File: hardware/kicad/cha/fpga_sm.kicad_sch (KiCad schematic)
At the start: 26 parts, among them J3 CONF SM, U14 iCE40HX4K-TQ144, X2 25 MHz 3,3 V

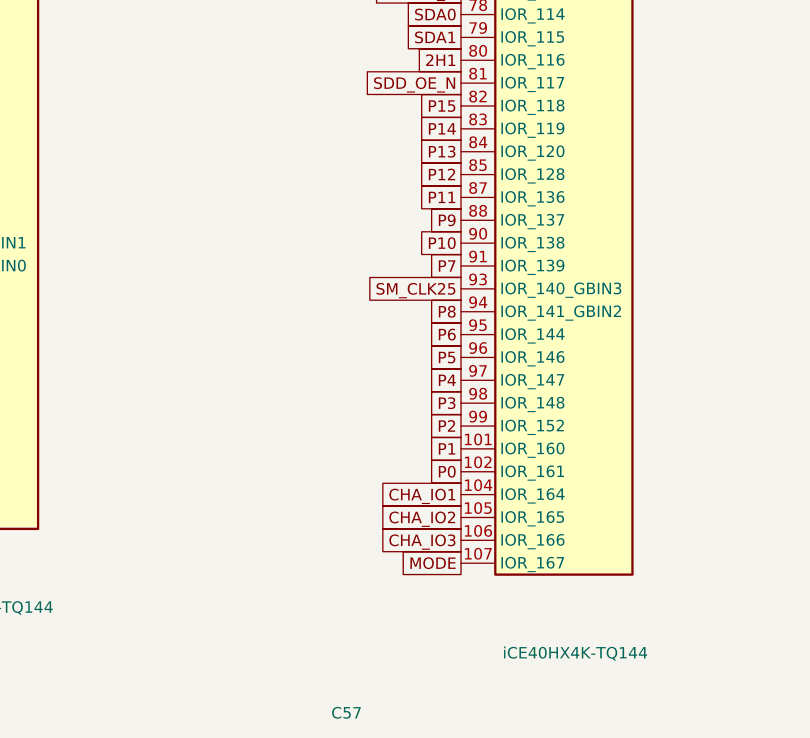
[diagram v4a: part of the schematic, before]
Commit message: Pico 2, microSD et bouton sur la carte PROG ; pistes d'alimentation larges
- La carte PROG est côté avant de la cartouche, composants vers l'avant :
  lecteur microSD et bouton accessibles. Le câble PROG-CHA porte
  désormais le bus de liaison C/SM ; connecteur au même endroit sur les
  deux cartes (x = 172 mm), prêt pour un connecteur carte à carte.
- Sous le Pico : ni piste ni via sur la face composants (pastilles de
  test nues sous le module).
- Classes de réseaux écrites dans le .kicad_pro : +5V et VSYS en 0,5 mm,
  +1V2 en 0,3 mm.
- Broches des FPGA réoptimisées ; contrôle Freerouting sans violation ;
  routage des deux cartes et vérification de timing en cours.

Co-Authored-By: Claude Opus 5.5 <noreply@anthropic.com>
Claude-Session: https://claude.ai/code/session_01WKfXP1YJ8otGxZ5dsY6Agh
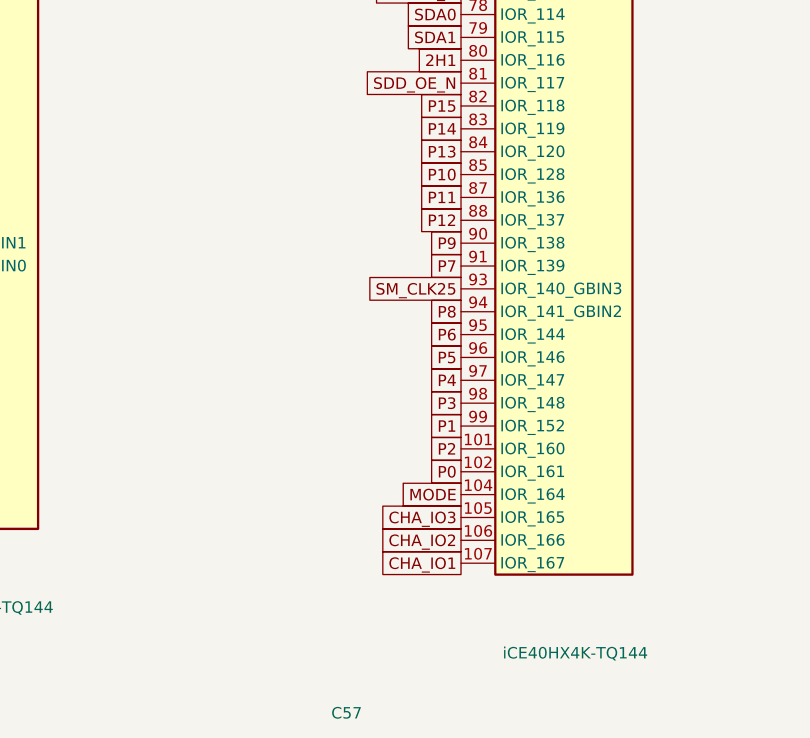
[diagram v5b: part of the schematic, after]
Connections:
- net CHA_IO1: now also U14.107 (IOR_167); no longer U14.104 (IOR_164)
- net CHA_IO2: now also U14.106 (IOR_166); no longer U14.105 (IOR_165)
- net CHA_IO3: now also U14.105 (IOR_165); no longer U14.106 (IOR_166)
- net MODE: now also U14.104 (IOR_164); no longer U14.107 (IOR_167)
- net P1: now also U14.99 (IOR_152); no longer U14.101 (IOR_160)
- net P10: now also U14.85 (IOR_128); no longer U14.90 (IOR_138)
- net P12: now also U14.88 (IOR_137); no longer U14.85 (IOR_128)
- net P2: now also U14.101 (IOR_160); no longer U14.99 (IOR_152)
- net P9: now also U14.90 (IOR_138); no longer U14.88 (IOR_137)
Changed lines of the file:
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@@
     (instances
       (project "cha"
-        (path "/c2acc1ad-3350-4022-8990-314ed37b470d/7c17e6ce-3dc1-4363-ae9a-1efd42617669"
+        (path "/e0c94673-4de7-4c3d-ae38-3ad172bd9211/19c2e398-814e-49a6-a22b-587549b2e82f"
           (reference "U14")
           (unit 1)))))
@@
     (instances
       (project "cha"
-        (path "/c2acc1ad-3350-4022-8990-314ed37b470d/7c17e6ce-3dc1-4363-ae9a-1efd42617669"
+        (path "/e0c94673-4de7-4c3d-ae38-3ad172bd9211/19c2e398-814e-49a6-a22b-587549b2e82f"
           (reference "U14")
           (unit 2)))))
@@
         (font
           (size 1.27 1.27)) hide)))
-  (global_label "P1"
+  (global_label "P2"
     (shape passive)
     (at 121.92 111.76 180)
@@
         (font
           (size 1.27 1.27)) hide)))
-  (global_label "CHA_IO1"
+  (global_label "MODE"
     (shape passive)
     (at 121.92 116.84 180)
@@
         (font
           (size 1.27 1.27)) hide)))
-  (global_label "CHA_IO2"
+  (global_label "CHA_IO3"
     (shape passive)
     (at 121.92 119.38 180)
@@
         (font
           (size 1.27 1.27)) hide)))
-  (global_label "CHA_IO3"
+  (global_label "CHA_IO2"
     (shape passive)
     (at 121.92 121.92 180)
@@
         (font
           (size 1.27 1.27)) hide)))
-  (global_label "MODE"
+  (global_label "CHA_IO1"
     (shape passive)
     (at 121.92 124.46 180)
@@
         (font
           (size 1.27 1.27)) hide)))
-  (global_label "P12"
+  (global_label "P10"
     (shape passive)
     (at 121.92 81.28 180)
@@
         (font
           (size 1.27 1.27)) hide)))
-  (global_label "P9"
+  (global_label "P12"
     (shape passive)
     (at 121.92 86.36 180)
@@
         (font
           (size 1.27 1.27)) hide)))
-  (global_label "P10"
+  (global_label "P9"
     (shape passive)
     (at 121.92 88.9 180)
@@
         (font
           (size 1.27 1.27)) hide)))
-  (global_label "P2"
+  (global_label "P1"
     (shape passive)
     (at 121.92 109.22 180)
@@
     (instances
       (project "cha"
-        (path "/c2acc1ad-3350-4022-8990-314ed37b470d/7c17e6ce-3dc1-4363-ae9a-1efd42617669"
+        (path "/e0c94673-4de7-4c3d-ae38-3ad172bd9211/19c2e398-814e-49a6-a22b-587549b2e82f"
           (reference "U14")
           (unit 3)))))
@@
     (instances
       (project "cha"
-        (path "/c2acc1ad-3350-4022-8990-314ed37b470d/7c17e6ce-3dc1-4363-ae9a-1efd42617669"
+        (path "/e0c94673-4de7-4c3d-ae38-3ad172bd9211/19c2e398-814e-49a6-a22b-587549b2e82f"
           (reference "U14")
           (unit 4)))))
@@
     (instances
       (project "cha"
-        (path "/c2acc1ad-3350-4022-8990-314ed37b470d/7c17e6ce-3dc1-4363-ae9a-1efd42617669"
+        (path "/e0c94673-4de7-4c3d-ae38-3ad172bd9211/19c2e398-814e-49a6-a22b-587549b2e82f"
           (reference "U14")
           (unit 5)))))
@@
     (instances
       (project "cha"
-        (path "/c2acc1ad-3350-4022-8990-314ed37b470d/7c17e6ce-3dc1-4363-ae9a-1efd42617669"
+        (path "/e0c94673-4de7-4c3d-ae38-3ad172bd9211/19c2e398-814e-49a6-a22b-587549b2e82f"
           (reference "C50")
           (unit 1)))))
@@
     (instances
       (project "cha"
-        (path "/c2acc1ad-3350-4022-8990-314ed37b470d/7c17e6ce-3dc1-4363-ae9a-1efd42617669"
+        (path "/e0c94673-4de7-4c3d-ae38-3ad172bd9211/19c2e398-814e-49a6-a22b-587549b2e82f"
           (reference "C51")
           (unit 1)))))
@@
     (instances
       (project "cha"
-        (path "/c2acc1ad-3350-4022-8990-314ed37b470d/7c17e6ce-3dc1-4363-ae9a-1efd42617669"
+        (path "/e0c94673-4de7-4c3d-ae38-3ad172bd9211/19c2e398-814e-49a6-a22b-587549b2e82f"
           (reference "C52")
           (unit 1)))))
@@
     (instances
       (project "cha"
-        (path "/c2acc1ad-3350-4022-8990-314ed37b470d/7c17e6ce-3dc1-4363-ae9a-1efd42617669"
+        (path "/e0c94673-4de7-4c3d-ae38-3ad172bd9211/19c2e398-814e-49a6-a22b-587549b2e82f"
           (reference "C53")
           (unit 1)))))
@@
     (instances
       (project "cha"
-        (path "/c2acc1ad-3350-4022-8990-314ed37b470d/7c17e6ce-3dc1-4363-ae9a-1efd42617669"
+        (path "/e0c94673-4de7-4c3d-ae38-3ad172bd9211/19c2e398-814e-49a6-a22b-587549b2e82f"
           (reference "C54")
           (unit 1)))))
@@
     (instances
       (project "cha"
-        (path "/c2acc1ad-3350-4022-8990-314ed37b470d/7c17e6ce-3dc1-4363-ae9a-1efd42617669"
+        (path "/e0c94673-4de7-4c3d-ae38-3ad172bd9211/19c2e398-814e-49a6-a22b-587549b2e82f"
           (reference "C55")
           (unit 1)))))
@@
     (instances
       (project "cha"
-        (path "/c2acc1ad-3350-4022-8990-314ed37b470d/7c17e6ce-3dc1-4363-ae9a-1efd42617669"
+        (path "/e0c94673-4de7-4c3d-ae38-3ad172bd9211/19c2e398-814e-49a6-a22b-587549b2e82f"
           (reference "C56")
           (unit 1)))))
@@
     (instances
       (project "cha"
-        (path "/c2acc1ad-3350-4022-8990-314ed37b470d/7c17e6ce-3dc1-4363-ae9a-1efd42617669"
+        (path "/e0c94673-4de7-4c3d-ae38-3ad172bd9211/19c2e398-814e-49a6-a22b-587549b2e82f"
           (reference "C57")
           (unit 1)))))
@@
     (instances
       (project "cha"
-        (path "/c2acc1ad-3350-4022-8990-314ed37b470d/7c17e6ce-3dc1-4363-ae9a-1efd42617669"
+        (path "/e0c94673-4de7-4c3d-ae38-3ad172bd9211/19c2e398-814e-49a6-a22b-587549b2e82f"
           (reference "C58")
           (unit 1)))))
@@
     (instances
       (project "cha"
-        (path "/c2acc1ad-3350-4022-8990-314ed37b470d/7c17e6ce-3dc1-4363-ae9a-1efd42617669"
+        (path "/e0c94673-4de7-4c3d-ae38-3ad172bd9211/19c2e398-814e-49a6-a22b-587549b2e82f"
           (reference "C59")
           (unit 1)))))
@@
     (instances
       (project "cha"
-        (path "/c2acc1ad-3350-4022-8990-314ed37b470d/7c17e6ce-3dc1-4363-ae9a-1efd42617669"
+        (path "/e0c94673-4de7-4c3d-ae38-3ad172bd9211/19c2e398-814e-49a6-a22b-587549b2e82f"
           (reference "C60")
           (unit 1)))))
@@
     (instances
       (project "cha"
-        (path "/c2acc1ad-3350-4022-8990-314ed37b470d/7c17e6ce-3dc1-4363-ae9a-1efd42617669"
+        (path "/e0c94673-4de7-4c3d-ae38-3ad172bd9211/19c2e398-814e-49a6-a22b-587549b2e82f"
           (reference "C61")
           (unit 1)))))
@@
     (instances
       (project "cha"
-        (path "/c2acc1ad-3350-4022-8990-314ed37b470d/7c17e6ce-3dc1-4363-ae9a-1efd42617669"
+        (path "/e0c94673-4de7-4c3d-ae38-3ad172bd9211/19c2e398-814e-49a6-a22b-587549b2e82f"
           (reference "C62")
           (unit 1)))))
@@
     (instances
       (project "cha"
-        (path "/c2acc1ad-3350-4022-8990-314ed37b470d/7c17e6ce-3dc1-4363-ae9a-1efd42617669"
+        (path "/e0c94673-4de7-4c3d-ae38-3ad172bd9211/19c2e398-814e-49a6-a22b-587549b2e82f"
           (reference "C63")
           (unit 1)))))
@@
     (instances
       (project "cha"
-        (path "/c2acc1ad-3350-4022-8990-314ed37b470d/7c17e6ce-3dc1-4363-ae9a-1efd42617669"
+        (path "/e0c94673-4de7-4c3d-ae38-3ad172bd9211/19c2e398-814e-49a6-a22b-587549b2e82f"
           (reference "C64")
           (unit 1)))))
@@
     (instances
       (project "cha"
-        (path "/c2acc1ad-3350-4022-8990-314ed37b470d/7c17e6ce-3dc1-4363-ae9a-1efd42617669"
+        (path "/e0c94673-4de7-4c3d-ae38-3ad172bd9211/19c2e398-814e-49a6-a22b-587549b2e82f"
           (reference "R10")
           (unit 1)))))
@@
     (instances
       (project "cha"
-        (path "/c2acc1ad-3350-4022-8990-314ed37b470d/7c17e6ce-3dc1-4363-ae9a-1efd42617669"
+        (path "/e0c94673-4de7-4c3d-ae38-3ad172bd9211/19c2e398-814e-49a6-a22b-587549b2e82f"
           (reference "C65")
           (unit 1)))))
@@
     (instances
       (project "cha"
-        (path "/c2acc1ad-3350-4022-8990-314ed37b470d/7c17e6ce-3dc1-4363-ae9a-1efd42617669"
+        (path "/e0c94673-4de7-4c3d-ae38-3ad172bd9211/19c2e398-814e-49a6-a22b-587549b2e82f"
           (reference "C66")
           (unit 1)))))
@@
     (instances
       (project "cha"
-        (path "/c2acc1ad-3350-4022-8990-314ed37b470d/7c17e6ce-3dc1-4363-ae9a-1efd42617669"
+        (path "/e0c94673-4de7-4c3d-ae38-3ad172bd9211/19c2e398-814e-49a6-a22b-587549b2e82f"
           (reference "R11")
           (unit 1)))))
@@
     (instances
       (project "cha"
-        (path "/c2acc1ad-3350-4022-8990-314ed37b470d/7c17e6ce-3dc1-4363-ae9a-1efd42617669"
+        (path "/e0c94673-4de7-4c3d-ae38-3ad172bd9211/19c2e398-814e-49a6-a22b-587549b2e82f"
           (reference "C67")
           (unit 1)))))
@@
     (instances
       (project "cha"
-        (path "/c2acc1ad-3350-4022-8990-314ed37b470d/7c17e6ce-3dc1-4363-ae9a-1efd42617669"
+        (path "/e0c94673-4de7-4c3d-ae38-3ad172bd9211/19c2e398-814e-49a6-a22b-587549b2e82f"
           (reference "C68")
           (unit 1)))))
@@
     (instances
       (project "cha"
-        (path "/c2acc1ad-3350-4022-8990-314ed37b470d/7c17e6ce-3dc1-4363-ae9a-1efd42617669"
+        (path "/e0c94673-4de7-4c3d-ae38-3ad172bd9211/19c2e398-814e-49a6-a22b-587549b2e82f"
           (reference "R12")
           (unit 1)))))
@@
     (instances
       (project "cha"
-        (path "/c2acc1ad-3350-4022-8990-314ed37b470d/7c17e6ce-3dc1-4363-ae9a-1efd42617669"
+        (path "/e0c94673-4de7-4c3d-ae38-3ad172bd9211/19c2e398-814e-49a6-a22b-587549b2e82f"
           (reference "J3")
           (unit 1)))))
@@
     (instances
       (project "cha"
-        (path "/c2acc1ad-3350-4022-8990-314ed37b470d/7c17e6ce-3dc1-4363-ae9a-1efd42617669"
+        (path "/e0c94673-4de7-4c3d-ae38-3ad172bd9211/19c2e398-814e-49a6-a22b-587549b2e82f"
           (reference "X2")
           (unit 1)))))
@@
     (instances
       (project "cha"
-        (path "/c2acc1ad-3350-4022-8990-314ed37b470d/7c17e6ce-3dc1-4363-ae9a-1efd42617669"
+        (path "/e0c94673-4de7-4c3d-ae38-3ad172bd9211/19c2e398-814e-49a6-a22b-587549b2e82f"
           (reference "C69")
           (unit 1)))))

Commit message: Régulateur 3,3 V à découpage, horloge SDRAM adaptée côté FPGA, U8 en 74AHCT125
- AP63203 (TSOT-23-6, sortie fixe 3,3 V, ~90 %) à la place de
  l'AMS1117 : ~0,15 W de pertes au lieu de ~0,75 W et moins de courant
  tiré sur le 5 V de la console ; L 4,7 µH, Cin 10 µF, Cout 2 x 22 µF.
- Résistance série de 33 ohms de l'horloge SDRAM déclarée avec le FPGA :
  placée à 2,7 mm de sa broche (au lieu de ~30 mm, côté SDRAM).
- CHA : U8 (16244 pour 2 canaux) remplacé par un 74AHCT125.
Cartes replacées, contrôle Freerouting sans violation ; routage des
deux cartes et vérification de timing en cours.

Co-Authored-By: Claude Opus 5.5 <noreply@anthropic.com>
Claude-Session: https://claude.ai/code/session_01WKfXP1YJ8otGxZ5dsY6Agh
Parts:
- removed C50: 100n, Capacitor_SMD:C_0603_1608Metric, symbol Device:C
- added C70: 100n, Capacitor_SMD:C_0603_1608Metric, symbol Device:C
- C54, C64, C67: value 10u -> 100n; footprint Capacitor_SMD:C_0805_2012Metric -> Capacitor_SMD:C_0603_1608Metric
- C55, C66, C68: value 100n -> 10u; footprint Capacitor_SMD:C_0603_1608Metric -> Capacitor_SMD:C_0805_2012Metric
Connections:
- net +1V2: now also C55.1
- net +3V3: now also C65.1, C70.1; no longer C55.1, C69.1
- net GND: now also C70.2
- net P1: now also U14.101 (IOR_160); no longer U14.99 (IOR_152)
- net P10: now also U14.90 (IOR_138); no longer U14.85 (IOR_128)
- net P12: now also U14.85 (IOR_128); no longer U14.88 (IOR_137)
- net P2: now also U14.99 (IOR_152); no longer U14.101 (IOR_160)
- net P9: now also U14.88 (IOR_137); no longer U14.90 (IOR_138)
- net SM_VCCPLL0: now also C67.1; no longer C65.1
- net SM_VCCPLL1: now also C69.1; no longer C67.1

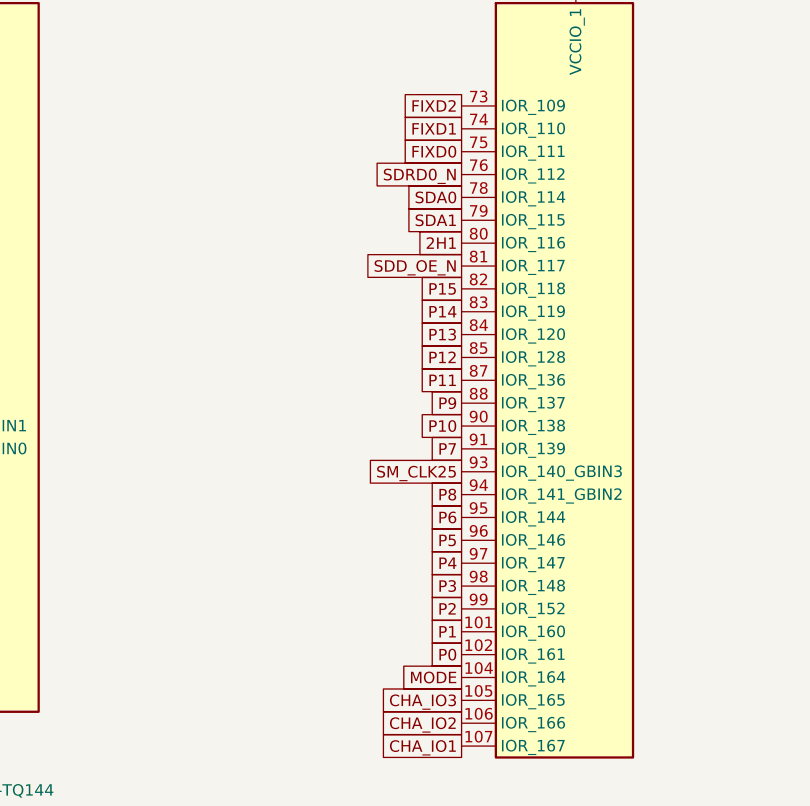
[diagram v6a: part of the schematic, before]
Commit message: CHA : canaux des tampons d'entrée groupés par FPGA de destination
SM seul (bus Z80, PCK2B, 2H1) à gauche, bus P0-P15 au milieu, C seul à
droite, chaque groupe dans l'ordre des contacts : le faisceau SDA entre
le FPGA SM et U3 ne se croise plus avec les signaux du FPGA C (SDA4
restait non routable). Carte CHA replacée, broches réoptimisées,
contrôle Freerouting sans violation ; routage en cours.

Co-Authored-By: Claude Opus 5.5 <noreply@anthropic.com>
Claude-Session: https://claude.ai/code/session_01WKfXP1YJ8otGxZ5dsY6Agh
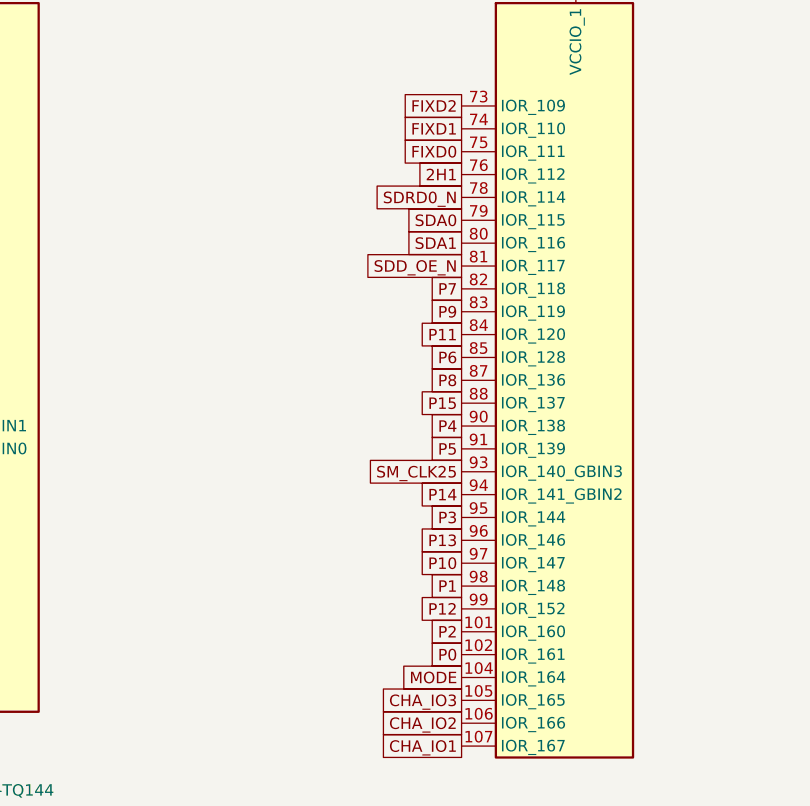
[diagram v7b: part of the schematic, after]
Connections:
- net 2H1: now also U14.76 (IOR_112); no longer U14.80 (IOR_116)
- net P1: now also U14.98 (IOR_148); no longer U14.101 (IOR_160)
- net P10: now also U14.97 (IOR_147); no longer U14.90 (IOR_138)
- net P11: now also U14.84 (IOR_120); no longer U14.87 (IOR_136)
- net P12: now also U14.99 (IOR_152); no longer U14.85 (IOR_128)
- net P13: now also U14.96 (IOR_146); no longer U14.84 (IOR_120)
- net P14: now also U14.94 (IOR_141_GBIN2); no longer U14.83 (IOR_119)
- net P15: now also U14.88 (IOR_137); no longer U14.82 (IOR_118)
- net P2: now also U14.101 (IOR_160); no longer U14.99 (IOR_152)
- net P3: now also U14.95 (IOR_144); no longer U14.98 (IOR_148)
- net P4: now also U14.90 (IOR_138); no longer U14.97 (IOR_147)
- net P5: now also U14.91 (IOR_139); no longer U14.96 (IOR_146)
- net P6: now also U14.85 (IOR_128); no longer U14.95 (IOR_144)
- net P7: now also U14.82 (IOR_118); no longer U14.91 (IOR_139)
- net P8: now also U14.87 (IOR_136); no longer U14.94 (IOR_141_GBIN2)
- net P9: now also U14.83 (IOR_119); no longer U14.88 (IOR_137)
- net SDA0: now also U14.79 (IOR_115); no longer U14.78 (IOR_114)
- net SDA1: now also U14.80 (IOR_116); no longer U14.79 (IOR_115)
- net SDRD0_N: now also U14.78 (IOR_114); no longer U14.76 (IOR_112)
